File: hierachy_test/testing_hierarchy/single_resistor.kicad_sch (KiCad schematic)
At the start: 1 part

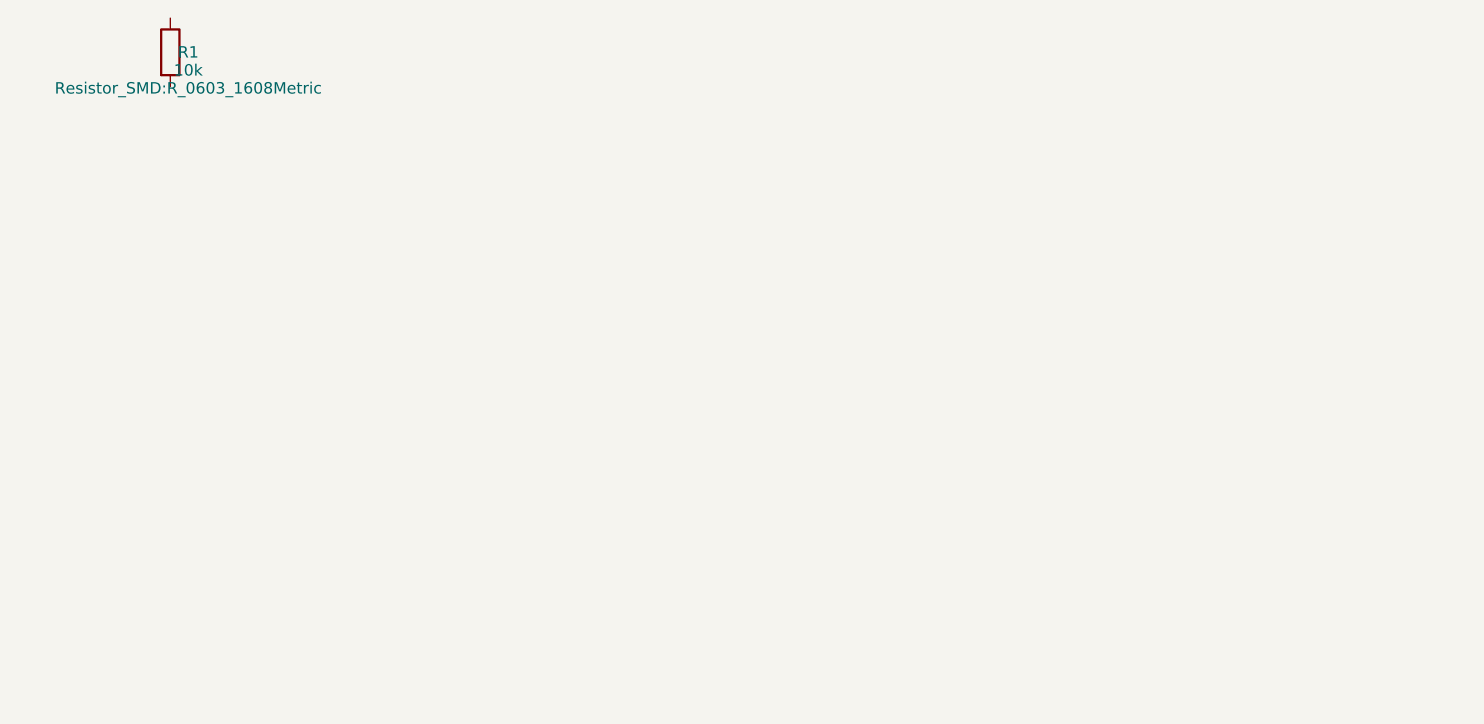
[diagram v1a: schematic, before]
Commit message: generating hierarchies, but not parts now
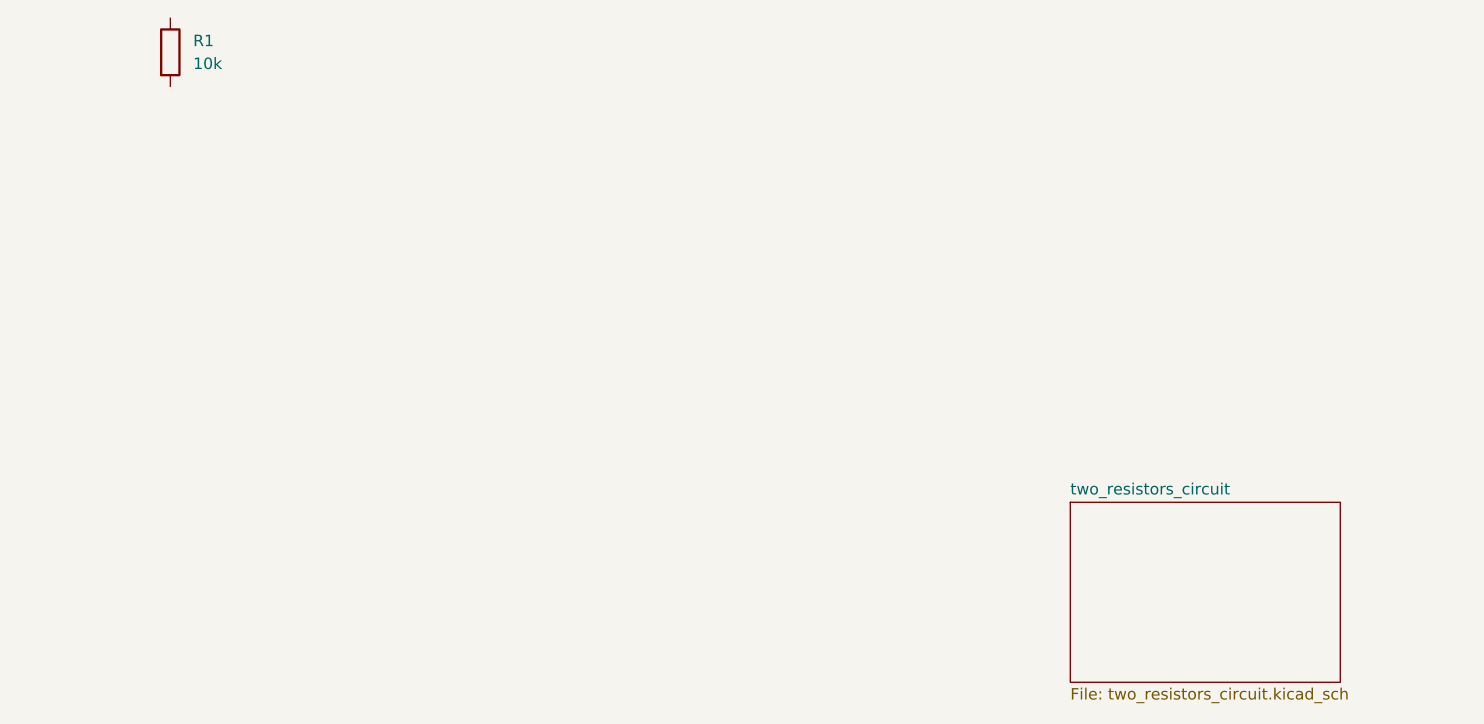
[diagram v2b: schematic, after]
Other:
- added sheet two_resistors_circuit (two_resistors_circuit.kicad_sch)
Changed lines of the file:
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@@
     (dnp no)
     (fields_autoplaced yes)
-    (property "Reference" "R1" (at 2.00 0.00 0))
-    (property "Value" "10k" (at 2.00 2.00 0))
-    (property "Footprint" "Resistor_SMD:R_0603_1608Metric" (at 2.00 4.00 0))
+    (property "Reference" "R1"
+      (at 2.54 -1.27 0)
+      (effects
+        (font
+          (size 1.27 1.27)
+        )
+        (justify left)
+      )
+    )
+    (property "Value" "10k"
+      (at 2.54 1.27 0)
+      (effects
+        (font
+          (size 1.27 1.27)
+        )
+        (justify left)
+      )
+    )
+    (property "Footprint" "Resistor_SMD:R_0603_1608Metric"
+      (at -1.78 0.00 90)
+      (effects
+        (font
+          (size 1.27 1.27)
+        )
+        (hide yes)
+      )
+    )
+    (property "Datasheet" "~"
+      (at 0.00 0.00 0)
+      (effects
+        (font
+          (size 1.27 1.27)
+        )
+        (hide yes)
+      )
+    )
+    (property "Description" "Resistor"
+      (at 0.00 0.00 0)
+      (effects
+        (font
+          (size 1.27 1.27)
+        )
+        (hide yes)
+      )
+    )
+    (pin "2"
+    )
+    (pin "1"
+    )
+    (instances
+      (project "testing_hierarchy"
+        (path "/"
+          (reference "R1")
+          (unit 1)
+        )
+      )
+    )
+  )
+  (sheet
+    (at 100 50)
+    (size 30 20)
+    (fields_autoplaced yes)
+    (stroke
+      (width 0.1524)
+      (type solid)
+    )
+    (fill
+      (color 0 0 0 0.0000)
+    )
+    (property "Sheetname" "two_resistors_circuit"
+      (at 100 49.2884 0)
+      (effects
+        (font
+          (size 1.27 1.27)
+        )
+        (justify left bottom)
+      )
+    )
+    (property "Sheetfile" "two_resistors_circuit.kicad_sch"
+      (at 100 70.5846 0)
+      (effects
+        (font
+          (size 1.27 1.27)
+        )
+        (justify left top)
+      )
+    )
+    (instances
+      (project "testing_hierarchy"
+        (path "/single_resistor/two_resistors_circuit"
+          (page "3")
+        )
+      )
+    )
   )
   (sheet_instances
     (path "/" (page "1"))
+    (path "/single_resistor/two_resistors_circuit" (page "0b856017-f205-49ce-abad-4f8850151966"))
   )
 )
